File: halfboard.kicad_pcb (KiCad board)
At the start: 2 copper layers, 240.1 x 87.9 mm, 54 parts, among them U1 

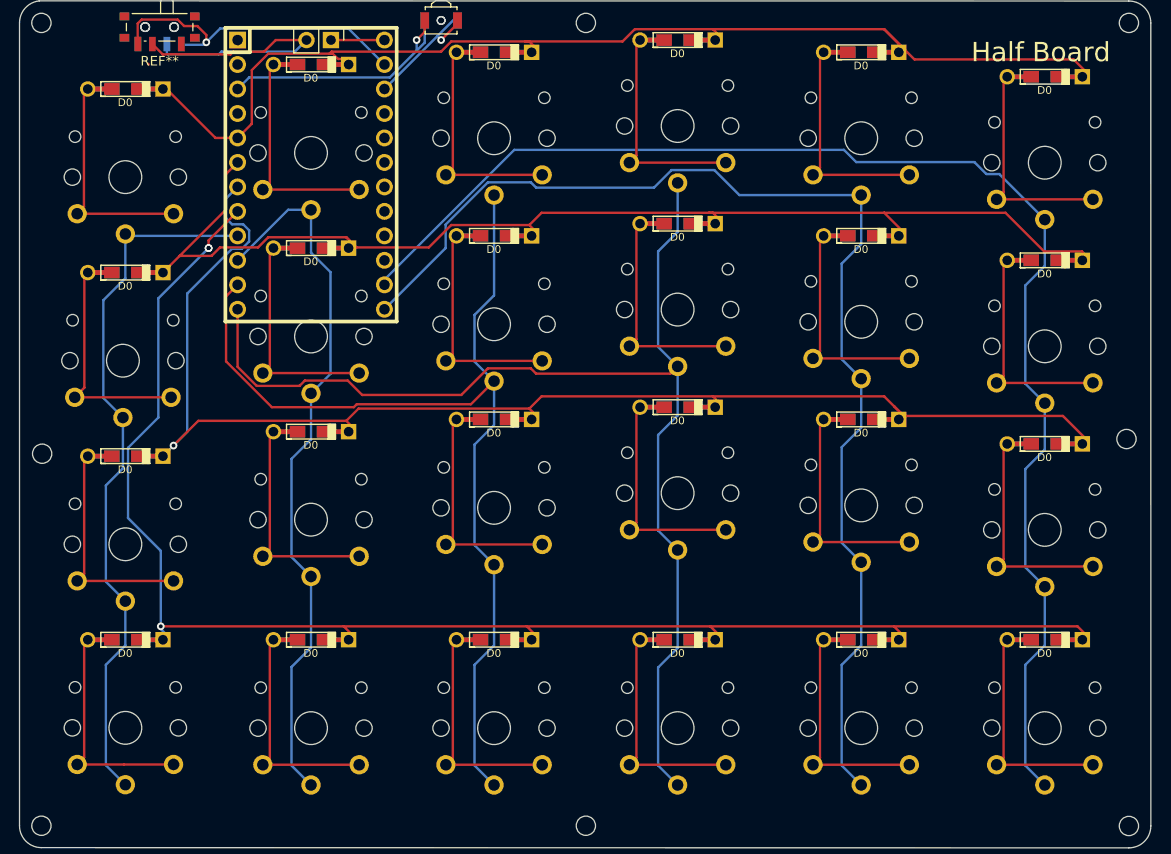
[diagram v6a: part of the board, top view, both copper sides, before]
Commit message: update switch footpring to support v2
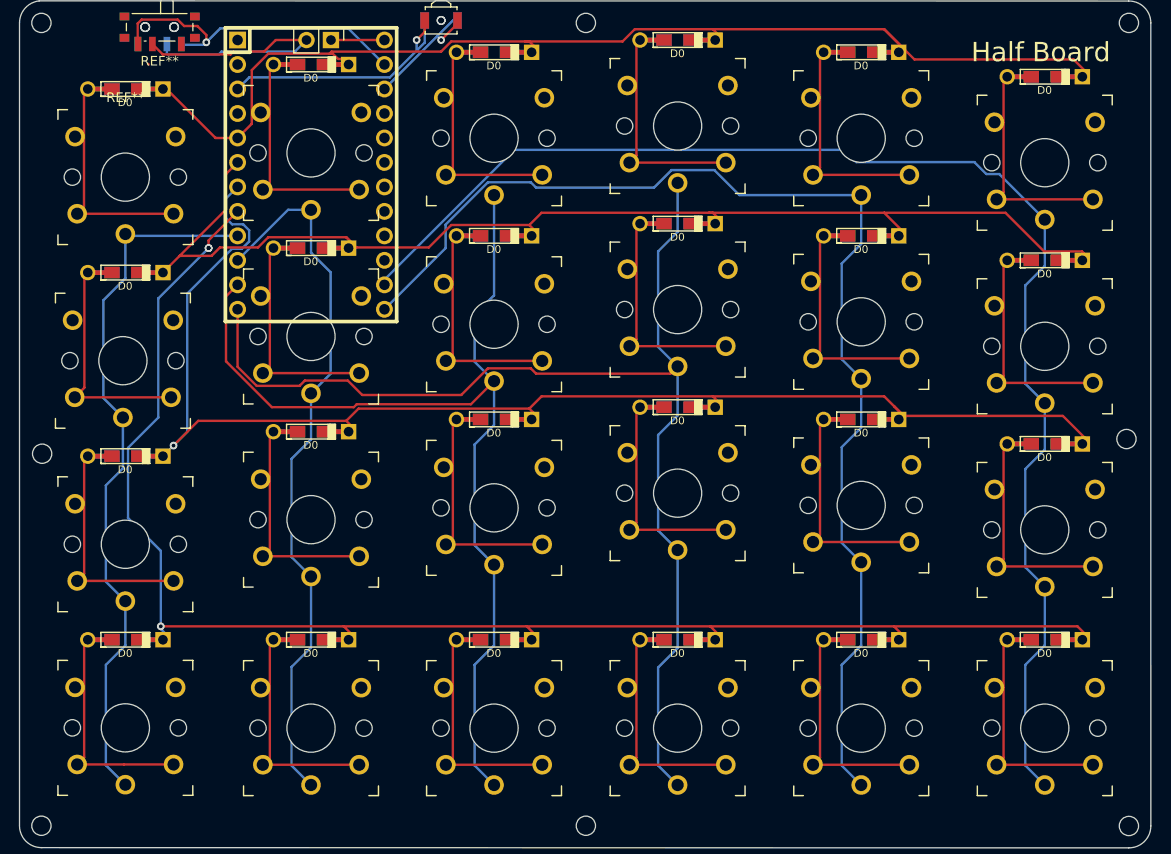
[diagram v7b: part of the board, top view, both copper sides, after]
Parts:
- removed the   at (125.4, 78.8)
- removed the   at (125.4, 59.7)
- removed the   at (106.3, 58.4)
- removed the   at (106.3, 77.5)
- removed the   at (106.3, 96.5)
- removed the   at (87.3, 98.1)
- removed the   at (87.3, 79.0)
- removed the   at (87.3, 59.7)
- removed the   at (68.3, 61.2)
- removed the   at (68.3, 80.3)
- removed the   at (144.4, 62.3)
- removed the   at (68.3, 99.3)
- removed the   at (68.3, 120.9)
- removed the   at (49.0, 120.9)
- removed the   at (49.0, 101.9)
- removed the   at (49.0, 63.8)
- removed the   at (144.4, 81.3)
- removed the   at (144.4, 100.4)
- removed the   at (144.4, 120.9)
- removed the   at (125.4, 120.9)
- removed the   at (106.3, 120.9)
- removed the   at (87.3, 120.9)
- removed the   at (125.4, 97.8)
- removed the REF** at (52.6, 48.5) (x2)
- added  : , halfboard:SW_PG1350_reversible_noLED, F.Cu at (144.4, 62.3)
- added  : , halfboard:SW_PG1350_reversible_noLED, F.Cu at (125.4, 59.7)
- added  : , halfboard:SW_PG1350_reversible_noLED, F.Cu at (106.3, 58.4)
- added  : , halfboard:SW_PG1350_reversible_noLED, F.Cu at (106.3, 77.5)
- added  : , halfboard:SW_PG1350_reversible_noLED, F.Cu at (106.3, 96.5)
- added  : , halfboard:SW_PG1350_reversible_noLED, F.Cu at (87.3, 98.1)
- added  : , halfboard:SW_PG1350_reversible_noLED, F.Cu at (87.3, 79.0)
- added  : , halfboard:SW_PG1350_reversible_noLED, F.Cu at (87.3, 59.7)
- added  : , halfboard:SW_PG1350_reversible_noLED, F.Cu at (68.3, 61.2)
- added  : , halfboard:SW_PG1350_reversible_noLED, F.Cu at (68.3, 80.3)
- added  : , halfboard:SW_PG1350_reversible_noLED, F.Cu at (68.3, 99.3)
- added  : , halfboard:SW_PG1350_reversible_noLED, F.Cu at (144.4, 81.3)
- added  : , halfboard:SW_PG1350_reversible_noLED, F.Cu at (68.3, 120.9)
- added  : , halfboard:SW_PG1350_reversible_noLED, F.Cu at (49.0, 120.9)
- added  : , halfboard:SW_PG1350_reversible_noLED, F.Cu at (49.0, 101.9)
- added  : , halfboard:SW_PG1350_reversible_noLED, F.Cu at (144.4, 100.4)
- added  : , halfboard:SW_PG1350_reversible_noLED, F.Cu at (144.4, 120.9)
- added  : , halfboard:SW_PG1350_reversible_noLED, F.Cu at (125.4, 120.9)
- added  : , halfboard:SW_PG1350_reversible_noLED, F.Cu at (106.3, 120.9)
- added  : , halfboard:SW_PG1350_reversible_noLED, F.Cu at (87.3, 120.9)
- added  : , halfboard:SW_PG1350_reversible_noLED, F.Cu at (125.4, 97.8)
- added  : , halfboard:SW_PG1350_reversible_noLED, F.Cu at (125.4, 78.8)
- added REF**: SW_PG1350_reversible_noLED, halfboard:SW_PG1350_reversible_noLED, F.Cu at (49.0, 63.8)
- added REF**: SW_SPDT_PCM12, Button_Switch_SMD:SW_SPDT_PCM12, F.Cu at (52.6, 48.5)
- added REF**: SW_SPDT_PCM12, Button_Switch_SMD:SW_SPDT_PCM12, B.Cu at (52.6, 48.5)
-  : footprint mlp:Kailh-PG1350-1u-reversible-flip -> halfboard:SW_PG1350_reversible_noLED

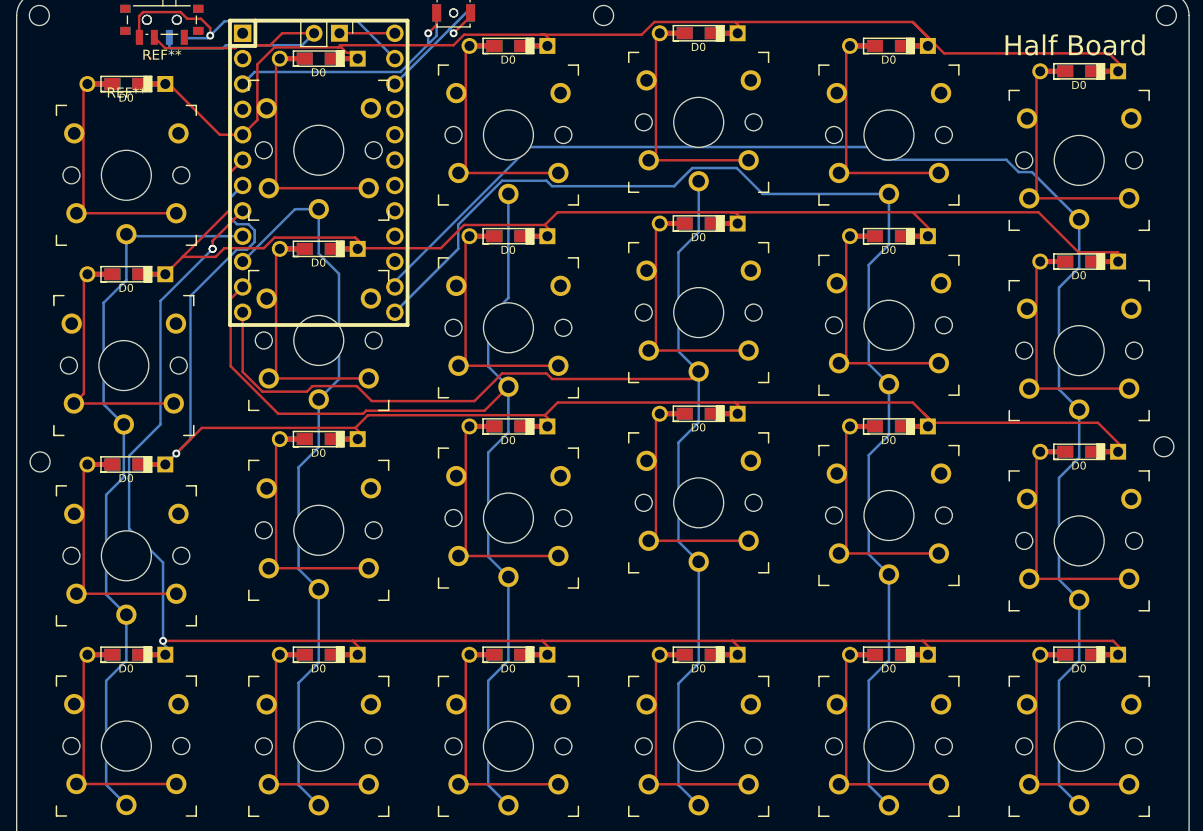
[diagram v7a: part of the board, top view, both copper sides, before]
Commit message: update switch footprint to support Choc v2
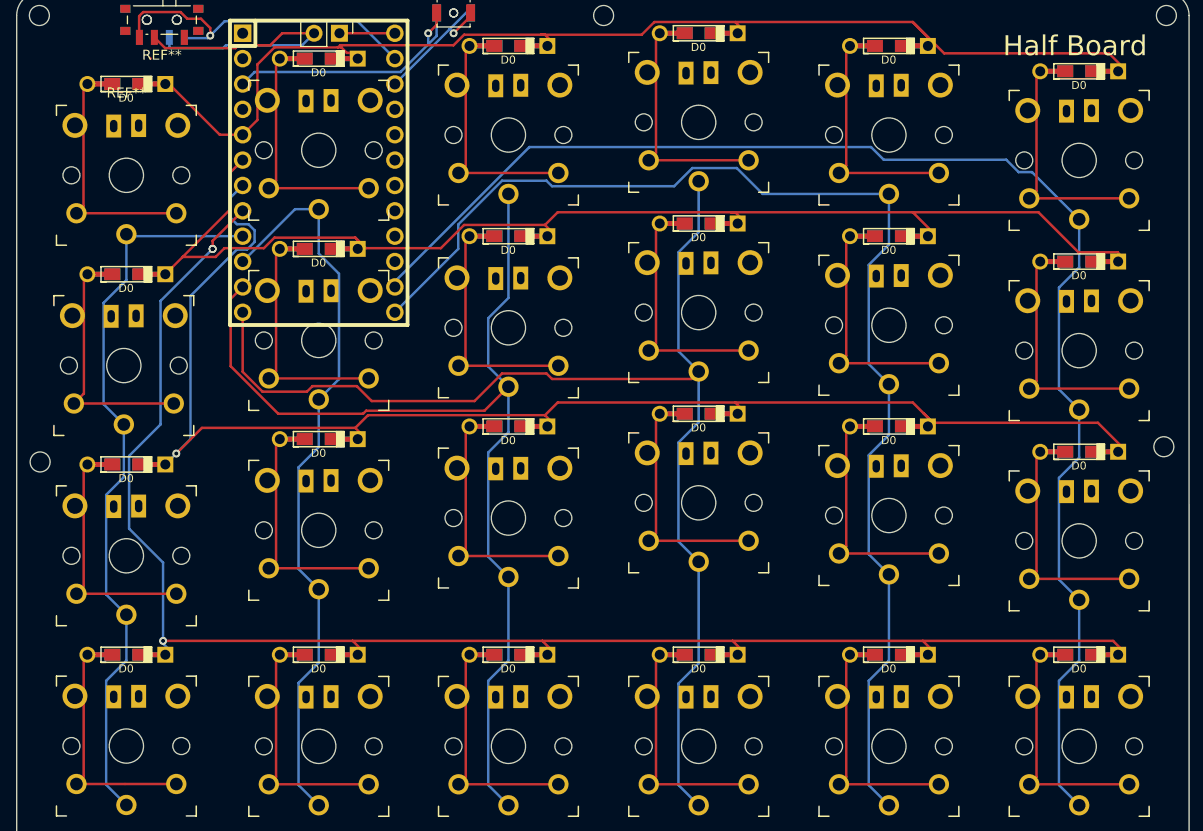
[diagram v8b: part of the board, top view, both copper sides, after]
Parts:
- removed the   at (144.4, 62.3)
- removed the   at (125.4, 59.7)
- removed the   at (106.3, 58.4)
- removed the   at (106.3, 77.5)
- removed the   at (106.3, 96.5)
- removed the   at (87.3, 98.1)
- removed the   at (87.3, 79.0)
- removed the   at (87.3, 59.7)
- removed the   at (68.3, 61.2)
- removed the   at (68.3, 80.3)
- removed the   at (68.3, 99.3)
- removed the   at (144.4, 81.3)
- removed the   at (68.3, 120.9)
- removed the   at (49.0, 120.9)
- removed the   at (49.0, 101.9)
- removed the   at (144.4, 100.4)
- removed the   at (144.4, 120.9)
- removed the   at (125.4, 120.9)
- removed the   at (106.3, 120.9)
- removed the   at (87.3, 120.9)
- removed the   at (125.4, 97.8)
- removed the   at (125.4, 78.8)
- removed the REF** at (52.6, 48.5) (x2)
- added  : , halfboard:SW_PG1350_reversible, F.Cu at (144.4, 62.3)
- added  : , halfboard:SW_PG1350_reversible, F.Cu at (125.4, 59.7)
- added  : , halfboard:SW_PG1350_reversible, F.Cu at (106.3, 58.4)
- added  : , halfboard:SW_PG1350_reversible, F.Cu at (106.3, 77.5)
- added  : , halfboard:SW_PG1350_reversible, F.Cu at (106.3, 96.5)
- added  : , halfboard:SW_PG1350_reversible, F.Cu at (87.3, 98.1)
- added  : , halfboard:SW_PG1350_reversible, F.Cu at (87.3, 79.0)
- added  : , halfboard:SW_PG1350_reversible, F.Cu at (87.3, 59.7)
- added  : , halfboard:SW_PG1350_reversible, F.Cu at (68.3, 61.2)
- added  : , halfboard:SW_PG1350_reversible, F.Cu at (68.3, 80.3)
- added  : , halfboard:SW_PG1350_reversible, F.Cu at (68.3, 99.3)
- added  : , halfboard:SW_PG1350_reversible, F.Cu at (144.4, 81.3)
- added  : , halfboard:SW_PG1350_reversible, F.Cu at (68.3, 120.9)
- added  : , halfboard:SW_PG1350_reversible, F.Cu at (49.0, 120.9)
- added  : , halfboard:SW_PG1350_reversible, F.Cu at (49.0, 101.9)
- added  : , halfboard:SW_PG1350_reversible, F.Cu at (144.4, 100.4)
- added  : , halfboard:SW_PG1350_reversible, F.Cu at (144.4, 120.9)
- added  : , halfboard:SW_PG1350_reversible, F.Cu at (125.4, 120.9)
- added  : , halfboard:SW_PG1350_reversible, F.Cu at (106.3, 120.9)
- added  : , halfboard:SW_PG1350_reversible, F.Cu at (87.3, 120.9)
- added  : , halfboard:SW_PG1350_reversible, F.Cu at (125.4, 97.8)
- added  : , halfboard:SW_PG1350_reversible, F.Cu at (125.4, 78.8)
- added REF**: SW_SPDT_PCM12, Button_Switch_SMD:SW_SPDT_PCM12, F.Cu at (52.6, 48.5)
- added REF**: SW_SPDT_PCM12, Button_Switch_SMD:SW_SPDT_PCM12, B.Cu at (52.6, 48.5)
-  : footprint halfboard:SW_PG1350_reversible_noLED -> halfboard:SW_PG1350_reversible
- REF**: value SW_PG1350_reversible_noLED -> SW_PG1350_reversible; footprint halfboard:SW_PG1350_reversible_noLED -> halfboard:SW_PG1350_reversible
